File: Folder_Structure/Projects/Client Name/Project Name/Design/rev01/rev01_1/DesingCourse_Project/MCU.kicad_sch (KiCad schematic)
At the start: 41 parts, among them J3 874380843, J4 874380343, J5 874380643, SW1 SW_DIP_x01, U3 STM32F405RGTx, Y1 8MHz

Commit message: Update13
Still working on FP for the MCU
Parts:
- removed Y1: 8MHz, symbol Device:Crystal
- added R64: 2k2, Resistor_SMD:R_0603_1608Metric, symbol Device:R
- added Y1: 8MHz, X50328MSB2GI:XTAL_MSB2GI_YXC, symbol X50328MSB2GI:X50328MSB2GI
- C10, C11, C12, C13, C16, C17, C18, C21, C7, C8: footprint (none) -> Capacitor_SMD:C_0603_1608Metric; Package (none) -> 0603; Temp Coeff (none) -> X7R; Tolerance (none) -> 10%; Voltage Rating (none) -> 10V
- C9: footprint (none) -> Capacitor_SMD:C_0603_1608Metric; Package (none) -> 0603; Temp Coeff (none) -> X5R; Tolerance (none) -> 10%; Voltage Rating (none) -> 10V
- FB1: value FerriteBead -> 120R; footprint (none) -> BLM18PG121SN1D:BEADC1608X95N; MPN (none) -> BLM18PG121SN1D; Manufacturer (none) -> Murata Electronics; Package (none) -> 0603
- R12, R13: value 2K2 -> 2k2; footprint (none) -> Resistor_SMD:R_0603_1608Metric; Package (none) -> 0603; Power Rating (none) -> 1/10W; Tolerance (none) -> 1%
- R19: footprint (none) -> Resistor_SMD:R_0603_1608Metric; Package (none) -> 0603; Power Rating (none) -> 1/10W; Tolerance (none) -> 1%
- SW1: value SW_DIP_x01 -> ~; footprint (none) -> PTS526SK15SMTR2LFS:SMT_FS; MPN (none) -> PTS526SK15SMTR2 LFS; Manufacturer (none) -> C&K; Package (none) -> SMT
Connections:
- net ADC_TEMP: now also R12.1; no longer R13.1
- net AN_IN: now also R13.1; no longer R12.1
- net GND: now also R64.2; no longer C10.2, SW1.1
- net P3V3: no longer C10.1
- net PH_0: now also Y1.2
- net PH_1: now also Y1.1
- new net: R64.1, SW1.1

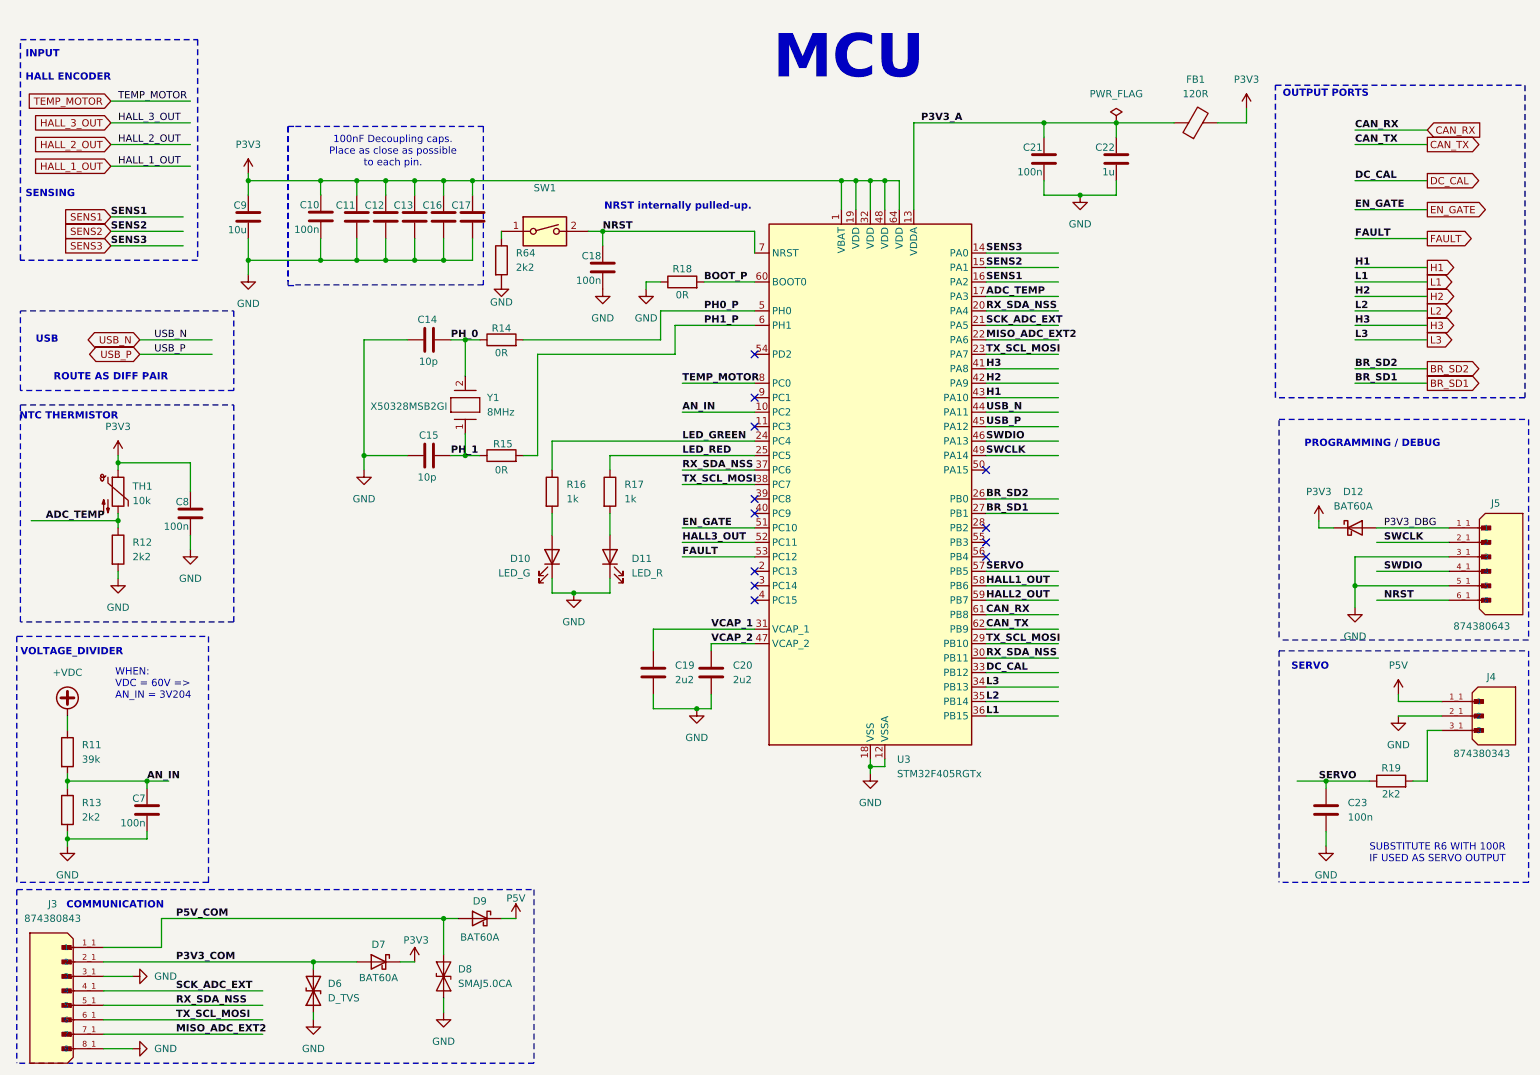
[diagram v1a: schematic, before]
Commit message: Update14
All components with FP, missing the block diagram
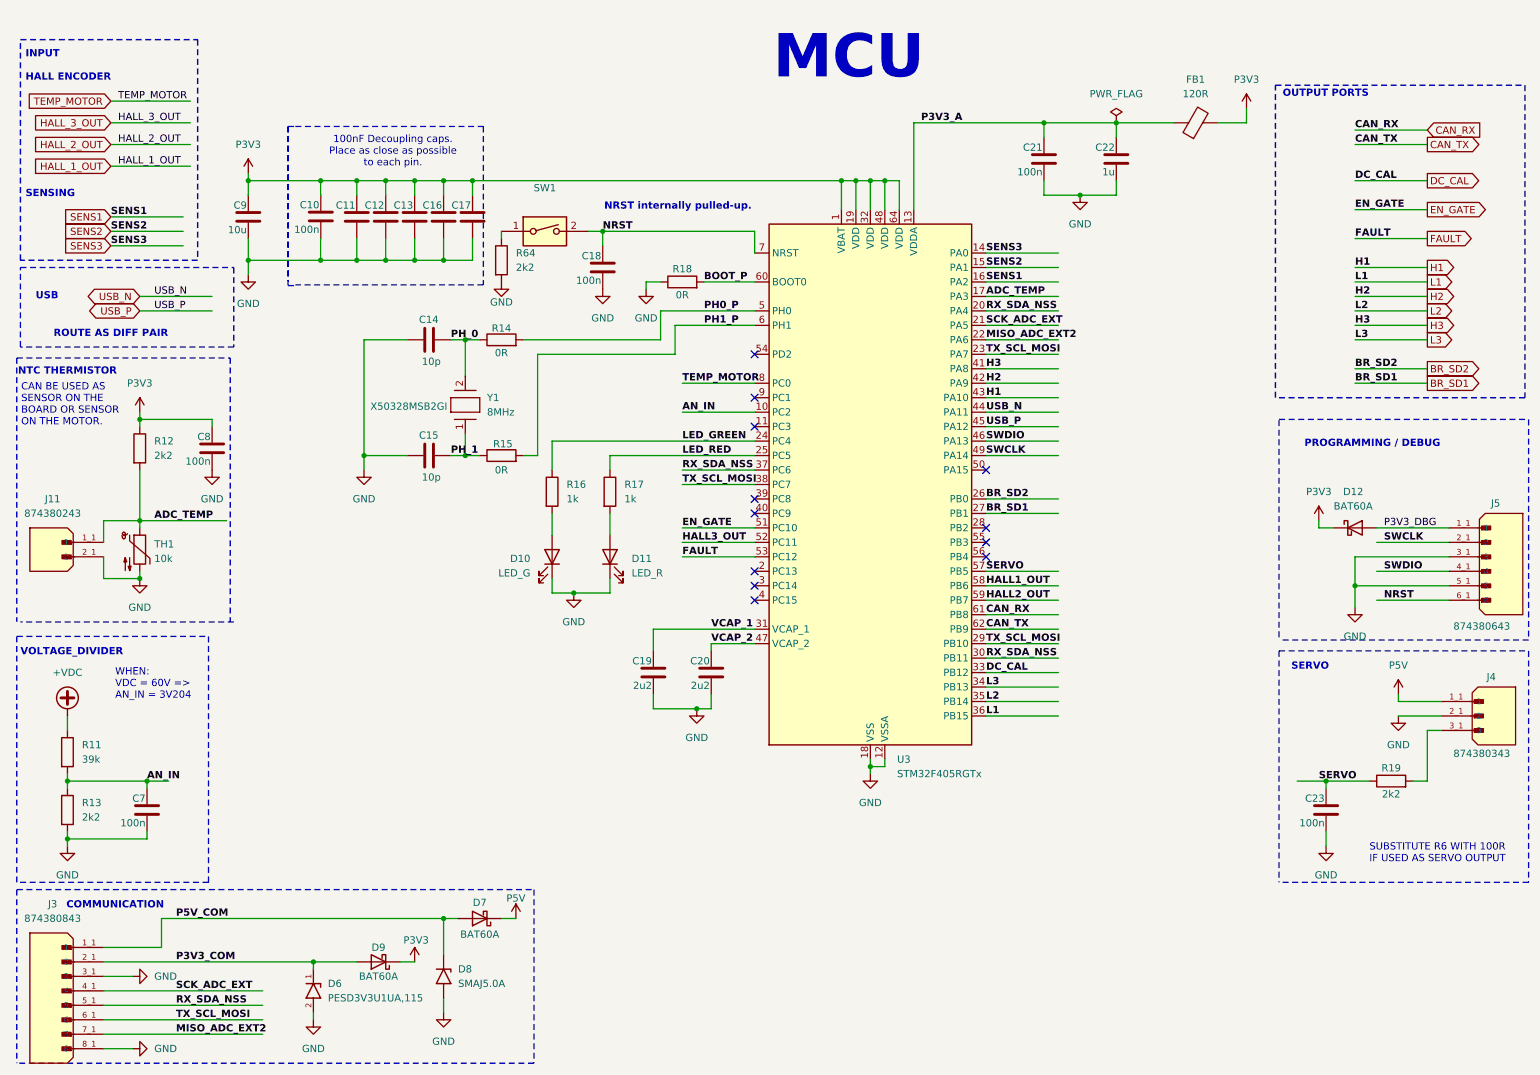
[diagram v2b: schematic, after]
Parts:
- removed D6: D_TVS, symbol Device:D_TVS
- removed D8: SMAJ5.0CA, SMAJ5.0CA:DIOM4325X250N, symbol JGB_Library:SMAJ5.0CA
- added D6: PESD3V3U1UA,115, PESD3V3U1UA_115:DIO_PESD3V3U1UA_115, symbol PESD3V3U1UA_115:PESD3V3U1UA_115
- added D8: SMAJ5.0A, Diode_SMD:D_SMA, symbol Diode:SMAJ5.0A
- added J11: 874380243, 874380843:MOLEX_874380243, symbol Molex_87438:874380243
- C14, C15: footprint (none) -> Capacitor_SMD:C_0603_1608Metric; Package (none) -> 0603; Temp Coeff (none) -> C0G/NP0; Tolerance (none) -> 10%; Voltage Rating (none) -> 50V
- C19, C20: footprint (none) -> Capacitor_SMD:C_0603_1608Metric; Package (none) -> 0603; Temp Coeff (none) -> X5R; Tolerance (none) -> 10%; Voltage Rating (none) -> 6.3V
- C23: footprint (none) -> Capacitor_SMD:C_0603_1608Metric; Package (none) -> 0603; Temp Coeff (none) -> X7R; Tolerance (none) -> 10%; Voltage Rating (none) -> 10V
- D12, D7, D9: MPN (none) -> BAT60A; Manufacturer (none) -> Infineon; Package (none) -> SOD-323
- TH1: footprint (none) -> Resistor_SMD:R_0603_1608Metric; MPN (none) -> NCP18XH103F03RB; Manufacturer (none) -> Murata Electronics; Package (none) -> 0603; Tolerance (none) -> 1%
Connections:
- net ADC_TEMP: now also R12.2, TH1.1, J11.1_1 (1), J11.1_2 (1); no longer R12.1, TH1.2
- net GND: now also TH1.2, D6.2, D8.2 (A2), J11.2_1 (2), J11.2_2 (2); no longer R12.2
- net P3V3: now also D9.1 (K), R12.1; no longer D7.1 (K), TH1.1
- net P3V3_COM: now also D9.2 (A), D6.1; no longer D7.2 (A)
- net P5V: now also D7.1 (K); no longer D9.1 (K)
- net P5V_COM: now also D7.2 (A), D8.1 (A1); no longer D9.2 (A)
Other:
- note added: "CAN BE USED AS SENSOR ON THE BOARD OR SENSOR ON THE MOTOR."
- moved on the sheet: C8, R12, TH1

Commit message: Update 16
Initial component placement done
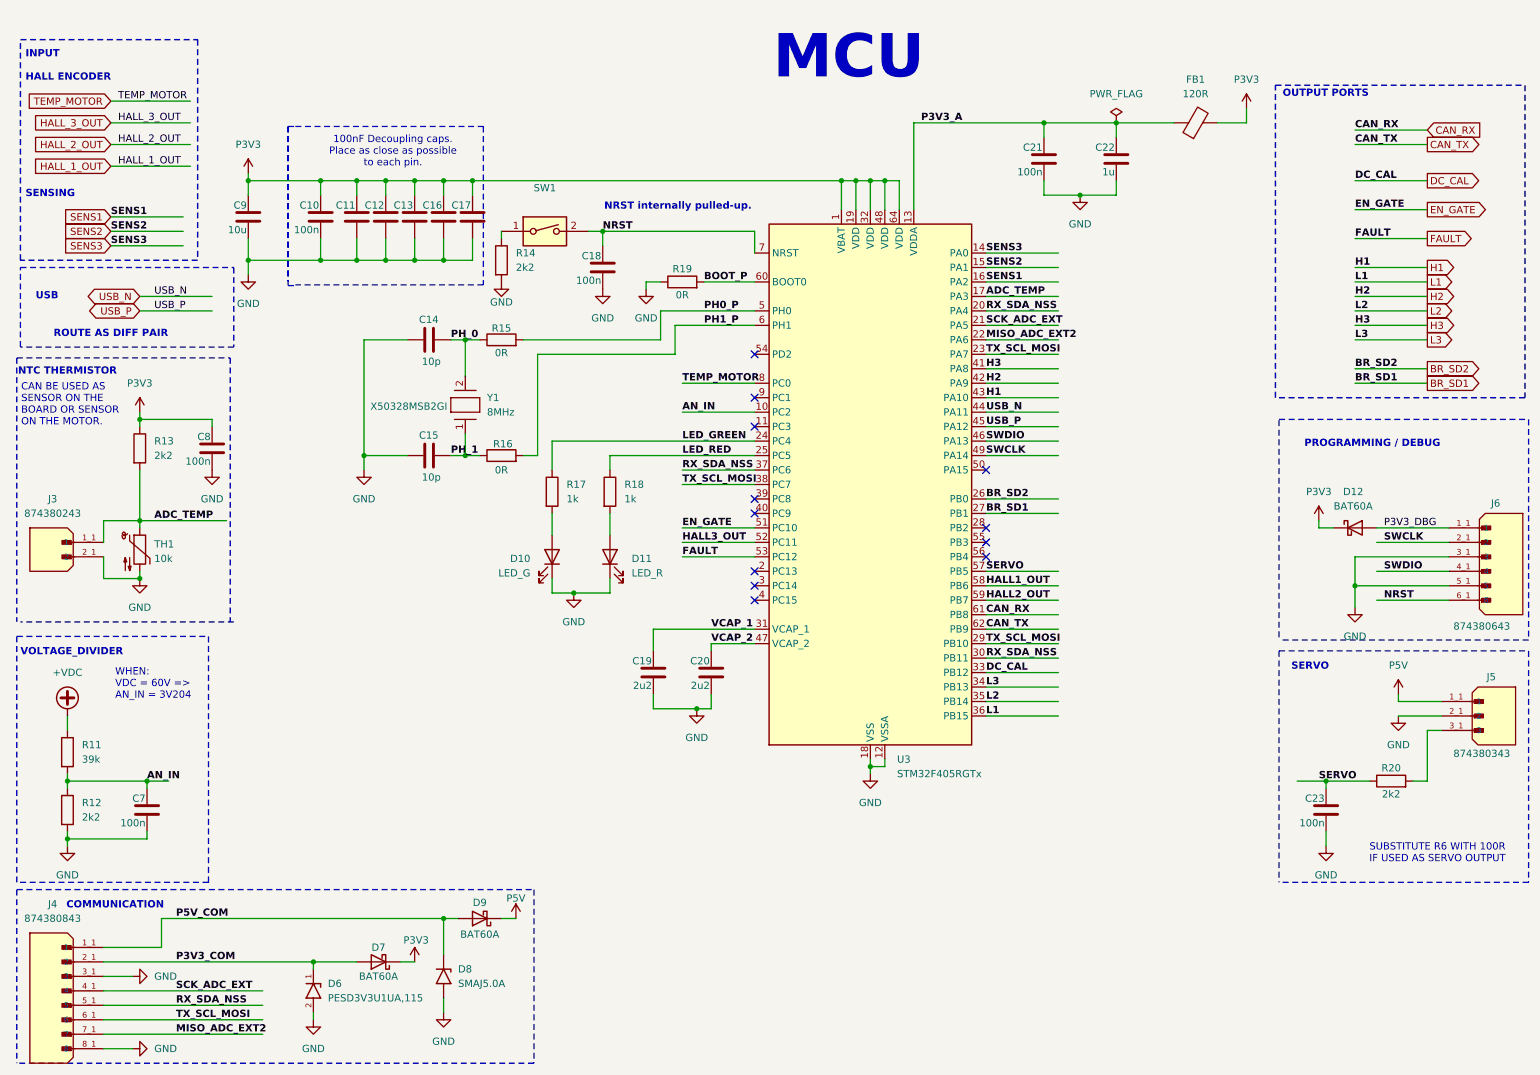
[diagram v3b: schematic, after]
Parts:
- D8: MPN (none) -> SMAJ5.0A; Manufacturer (none) -> Littelfuse; Package (none) -> DO-214AC
- U3: MPN (none) -> STM32F405RGTx; Manufacturer (none) -> STMicroelectronics; Package (none) -> LQFP64
- renumbered D9 to D7, D7 to D9, J11 to J3, J3 to J4, J4 to J5, J5 to J6, R13 to R12, R12 to R13, R64 to R14, R14 to R15, R15 to R16, R16 to R17, R17 to R18, R18 to R19, R19 to R20
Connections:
- net GND: now also C10.2
- net P3V3: now also C10.1

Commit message: Update17
Design rules and stack defined.

Check againg DR and proceed with layout.
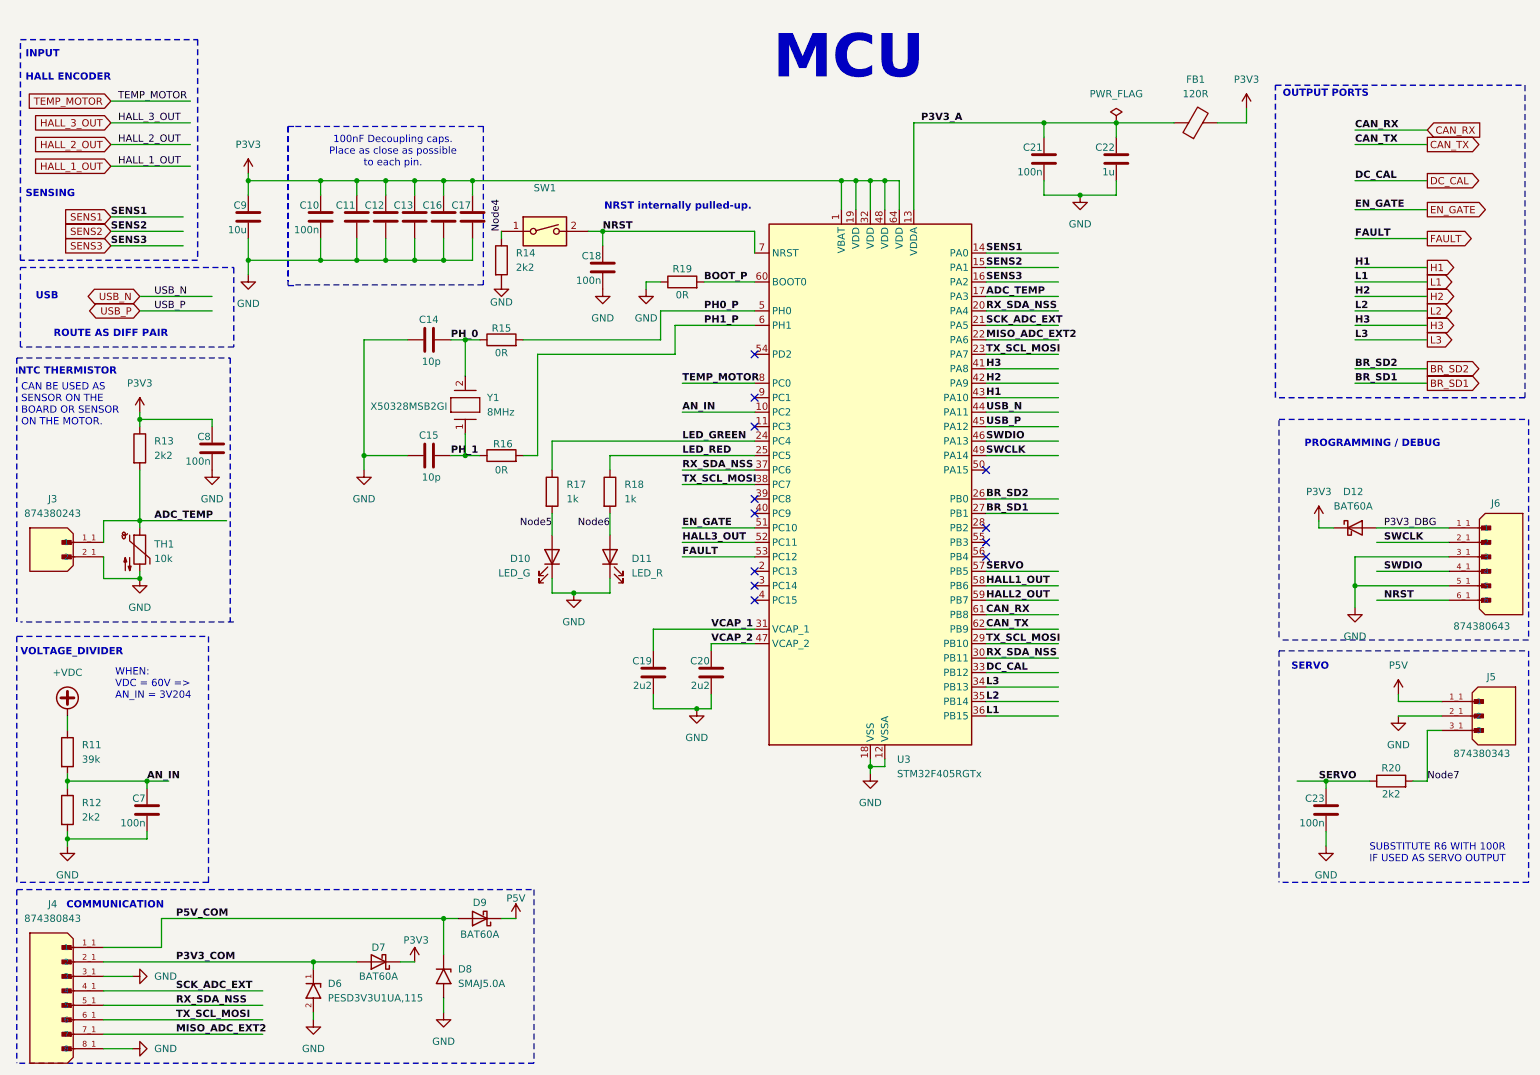
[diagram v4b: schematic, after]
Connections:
- net SENS1: now also U3.14 (PA0); no longer U3.16 (PA2)
- net SENS3: now also U3.16 (PA2); no longer U3.14 (PA0)
- net Node6: now reaches D11.2 (A), R18.2
- net Node4: now reaches R14.1, SW1.1
- net Node5: now reaches D10.2 (A), R17.2
- net Node7: now reaches J5.3_1 (3), J5.3_2 (3), R20.2
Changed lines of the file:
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@@
+		)
+	)
+	(label "Node7"
+		(at 261.62 147.32 0)
+		(effects
+			(font
+				(size 1.27 1.27)
+			)
+			(justify left bottom)
 		)
 	)
@@
 		)
 	)
+	(label "SENS1"
+		(at 184.15 54.61 0)
+		(effects
+			(font
+				(size 1.27 1.27)
+				(thickness 0.254)
+				(bold yes)
+			)
+			(justify left bottom)
+		)
+	)
 	(label "SWCLK"
 		(at 184.15 90.17 0)
@@
 		)
 	)
+	(label "Node5"
+		(at 107.95 102.87 180)
+		(effects
+			(font
+				(size 1.27 1.27)
+			)
+			(justify right bottom)
+		)
+	)
 	(label "HALL2_OUT"
 		(at 184.15 115.57 0)
@@
 		)
 	)
-	(label "SENS1"
-		(at 184.15 59.69 0)
-		(effects
-			(font
-				(size 1.27 1.27)
-				(thickness 0.254)
-				(bold yes)
-			)
-			(justify left bottom)
-		)
-	)
 	(label "EN_GATE"
 		(at 130.81 102.87 0)
@@
 		)
 	)
-	(label "SENS3"
-		(at 184.15 54.61 0)
-		(effects
-			(font
-				(size 1.27 1.27)
-				(thickness 0.254)
-				(bold yes)
-			)
-			(justify left bottom)
-		)
-	)
 	(label "BR_SD2"
 		(at 184.15 97.79 0)
@@
 		)
 	)
+	(label "SENS3"
+		(at 184.15 59.69 0)
+		(effects
+			(font
+				(size 1.27 1.27)
+				(thickness 0.254)
+				(bold yes)
+			)
+			(justify left bottom)
+		)
+	)
 	(label "HALL_2_OUT"
 		(at 31.75 35.56 0)
@@
 		)
 	)
+	(label "Node6"
+		(at 118.11 102.87 180)
+		(effects
+			(font
+				(size 1.27 1.27)
+			)
+			(justify right bottom)
+		)
+	)
 	(label "BR_SD1"
 		(at 184.15 100.33 0)
@@
 			)
 			(justify left bottom)
+		)
+	)
+	(label "Node4"
+		(at 99.06 50.8 90)
+		(effects
+			(font
+				(size 1.27 1.27)
+			)
+			(justify left bottom)
